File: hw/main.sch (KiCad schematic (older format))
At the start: 2 parts

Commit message: finished schematic
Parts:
- removed AE?: Antenna, symbol Device:Antenna
- removed U?: HM-TRP-869S, symbol KLIB_RF_Module:HM-TRP-869S
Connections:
- net labels removed: +3V3, GND
- wire segments 6 -> 67

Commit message: placement component to pcb
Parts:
- added H1, H2, H3, H4: M3, KLIB_Mechanical:Bolt_M3, symbol KLIB_Mechanical:Bolt
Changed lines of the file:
@@
 Wire Wire Line
 	2800 3900 3600 3900
+$Comp
+L KLIB_Mechanical:Bolt H1
+U 1 1 5AD47C00
+P 750 7650
+F 0 "H1" H 855 7721 50  0000 L CNN
+F 1 "M3" H 855 7630 50  0000 L CNN
+F 2 "KLIB_Mechanical:Bolt_M3" H 850 7500 50  0001 L CNN
+F 3 "~" H 875 7575 50  0001 C CNN
+	1    750  7650
+	1    0    0    -1
+$EndComp
+$Comp
+L KLIB_Mechanical:Bolt H2
+U 1 1 5AD47C90
+P 1100 7650
+F 0 "H2" H 1205 7721 50  0000 L CNN
+F 1 "M3" H 1205 7630 50  0000 L CNN
+F 2 "KLIB_Mechanical:Bolt_M3" H 1200 7500 50  0001 L CNN
+F 3 "~" H 1225 7575 50  0001 C CNN
+	1    1100 7650
+	1    0    0    -1
+$EndComp
+$Comp
+L KLIB_Mechanical:Bolt H3
+U 1 1 5AD47CA5
+P 1450 7650
+F 0 "H3" H 1555 7721 50  0000 L CNN
+F 1 "M3" H 1555 7630 50  0000 L CNN
+F 2 "KLIB_Mechanical:Bolt_M3" H 1550 7500 50  0001 L CNN
+F 3 "~" H 1575 7575 50  0001 C CNN
+	1    1450 7650
+	1    0    0    -1
+$EndComp
+$Comp
+L KLIB_Mechanical:Bolt H4
+U 1 1 5AD47CBC
+P 1800 7650
+F 0 "H4" H 1905 7721 50  0000 L CNN
+F 1 "M3" H 1905 7630 50  0000 L CNN
+F 2 "KLIB_Mechanical:Bolt_M3" H 1900 7500 50  0001 L CNN
+F 3 "~" H 1925 7575 50  0001 C CNN
+	1    1800 7650
+	1    0    0    -1
+$EndComp
 $EndSCHEMATC

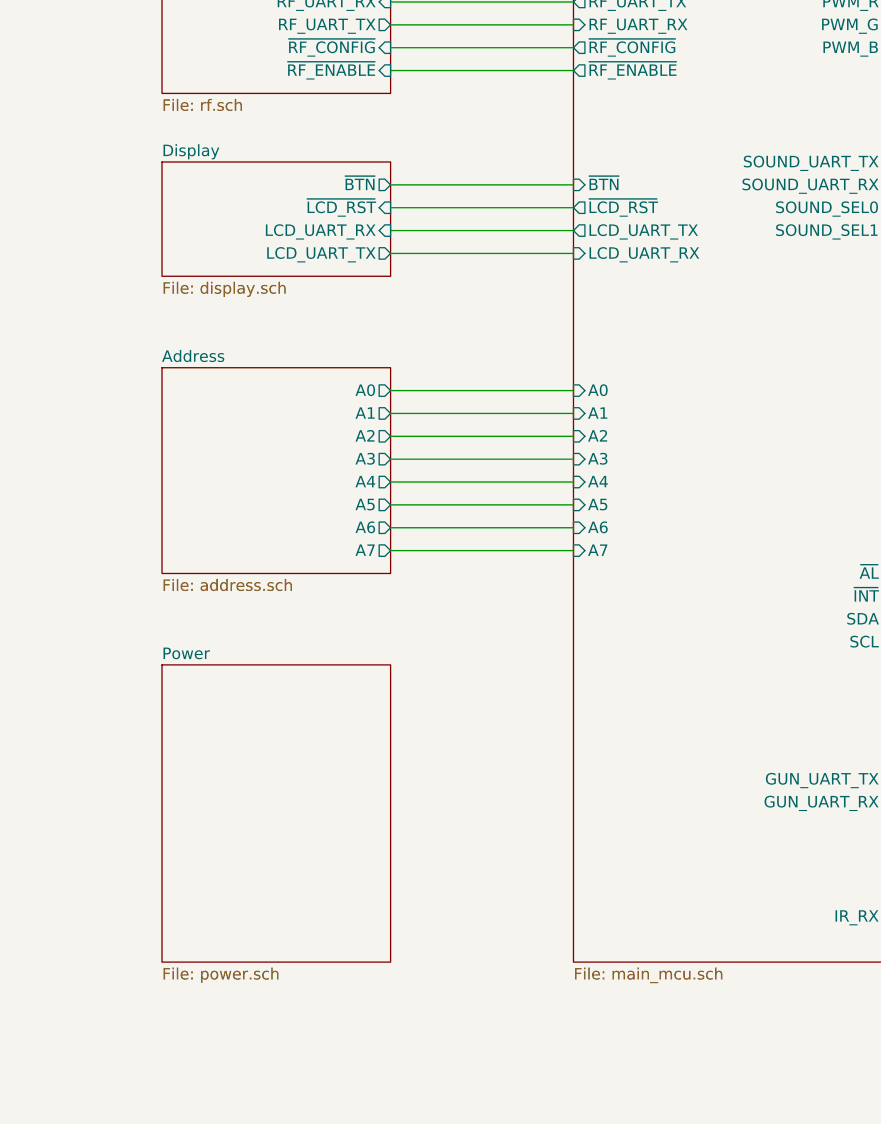
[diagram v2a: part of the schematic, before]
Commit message: removed LCD RST signal
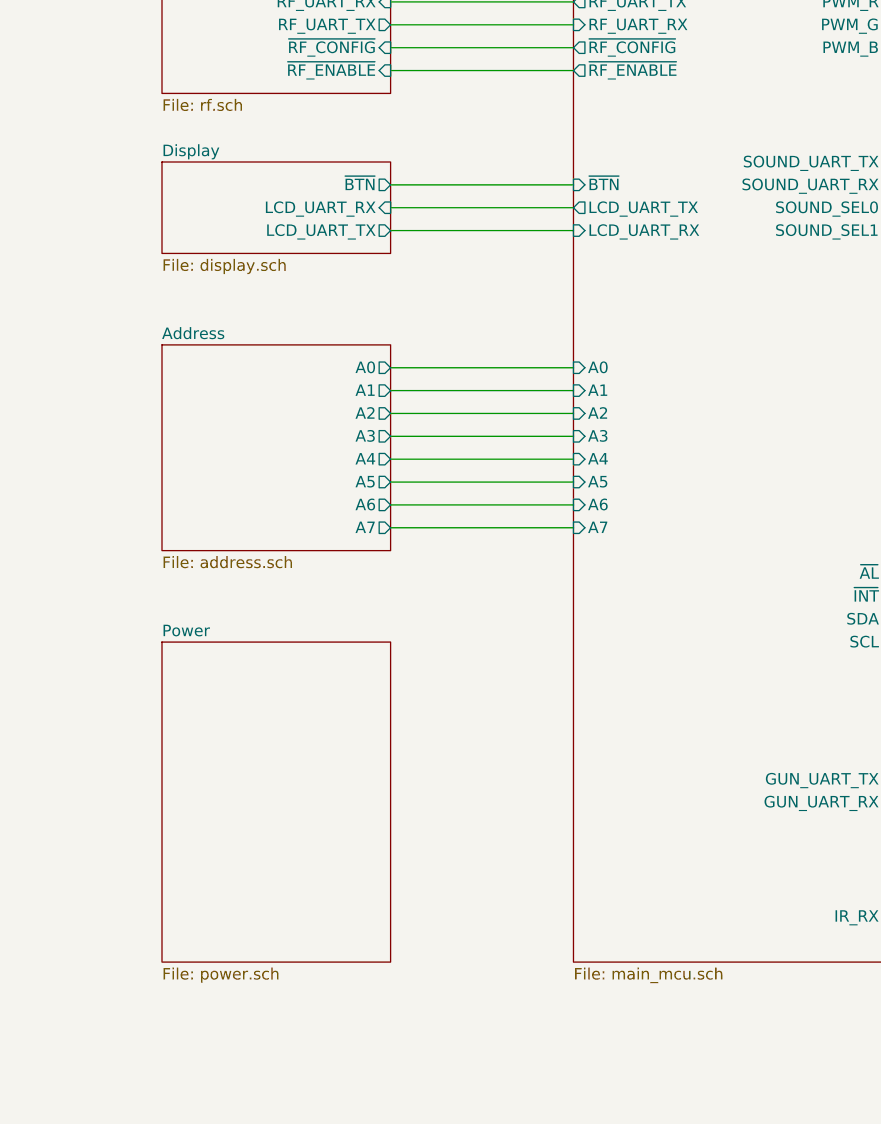
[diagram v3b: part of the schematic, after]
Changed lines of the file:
@@
 F6 "GUN_UART_TX" O R 5000 4900 50
 F7 "GUN_UART_RX" I R 5000 5000 50
-F8 "LCD_UART_TX" O L 3600 2500 50
-F9 "LCD_UART_RX" I L 3600 2600 50
+F8 "LCD_UART_TX" O L 3600 2400 50
+F9 "LCD_UART_RX" I L 3600 2500 50
 F10 "SOUND_UART_TX" O R 5000 2200 50
 F11 "SOUND_UART_RX" I R 5000 2300 50
 F12 "SOUND_SEL0" O R 5000 2400 50
 F13 "SOUND_SEL1" O R 5000 2500 50
-F14 "~LCD_RST" O L 3600 2400 50
-F15 "SDA" B R 5000 4200 50
-F16 "SCL" O R 5000 4300 50
-F17 "~AL" I R 5000 4000 50
-F18 "~INT" I R 5000 4100 50
-F19 "~BTN" I L 3600 2300 50
-F20 "PWM_R" O R 5000 1500 50
-F21 "PWM_G" O R 5000 1600 50
-F22 "A0" I L 3600 3200 50
-F23 "A1" I L 3600 3300 50
-F24 "A2" I L 3600 3400 50
-F25 "A3" I L 3600 3500 50
-F26 "A4" I L 3600 3600 50
-F27 "A5" I L 3600 3700 50
-F28 "A6" I L 3600 3800 50
-F29 "A7" I L 3600 3900 50
-F30 "PWM_B" O R 5000 1700 50
-F31 "IR_RX" I R 5000 5500 50
+F14 "SDA" B R 5000 4200 50
+F15 "SCL" O R 5000 4300 50
+F16 "~AL" I R 5000 4000 50
+F17 "~INT" I R 5000 4100 50
+F18 "~BTN" I L 3600 2300 50
+F19 "PWM_R" O R 5000 1500 50
+F20 "PWM_G" O R 5000 1600 50
+F21 "A0" I L 3600 3100 50
+F22 "A1" I L 3600 3200 50
+F23 "A2" I L 3600 3300 50
+F24 "A3" I L 3600 3400 50
+F25 "A4" I L 3600 3500 50
+F26 "A5" I L 3600 3600 50
+F27 "A6" I L 3600 3700 50
+F28 "A7" I L 3600 3800 50
+F29 "PWM_B" O R 5000 1700 50
+F30 "IR_RX" I R 5000 5500 50
 $EndSheet
 $Sheet
@@
 $EndSheet
 $Sheet
-S 1800 2200 1000 500
+S 1800 2200 1000 400
 U 5AD41C3E
 F0 "Display" 50
 F1 "display.sch" 50
-F2 "LCD_UART_TX" O R 2800 2600 50
-F3 "LCD_UART_RX" I R 2800 2500 50
-F4 "~LCD_RST" I R 2800 2400 50
-F5 "~BTN" O R 2800 2300 50
+F2 "LCD_UART_TX" O R 2800 2500 50
+F3 "LCD_UART_RX" I R 2800 2400 50
+F4 "~BTN" O R 2800 2300 50
 $EndSheet
 $Sheet
@@
 	7200 3200 8000 3200
 $Sheet
-S 1800 4400 1000 1300
+S 1800 4300 1000 1400
 U 5ACF814F
 F0 "Power" 50
@@
 	3600 2500 2800 2500
 Wire Wire Line
-	3600 2600 2800 2600
-Wire Wire Line
 	5000 2200 5800 2200
 Wire Wire Line
@@
 Connection ~ 10100 5500
 $Sheet
-S 1800 3100 1000 900
+S 1800 3000 1000 900
 U 5AD71AF2
 F0 "Address" 50
 F1 "address.sch" 50
-F2 "A0" O R 2800 3200 50
-F3 "A1" O R 2800 3300 50
-F4 "A2" O R 2800 3400 50
-F5 "A3" O R 2800 3500 50
-F6 "A4" O R 2800 3600 50
-F7 "A5" O R 2800 3700 50
-F8 "A6" O R 2800 3800 50
-F9 "A7" O R 2800 3900 50
-$EndSheet
+F2 "A0" O R 2800 3100 50
+F3 "A1" O R 2800 3200 50
+F4 "A2" O R 2800 3300 50
+F5 "A3" O R 2800 3400 50
+F6 "A4" O R 2800 3500 50
+F7 "A5" O R 2800 3600 50
+F8 "A6" O R 2800 3700 50
+F9 "A7" O R 2800 3800 50
+$EndSheet
+Wire Wire Line
+	2800 3100 3600 3100
 Wire Wire Line
 	2800 3200 3600 3200
@@
 Wire Wire Line
 	2800 3800 3600 3800
-Wire Wire Line
-	2800 3900 3600 3900
 $Comp
 L KLIB_Mechanical:Bolt H1
